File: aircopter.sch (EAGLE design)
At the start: 42 parts, among them IC1 STF202-22T1G, M1 WIRELESS-NRF24L01, U2 GY-521MPU6050, Y1 20 MHz

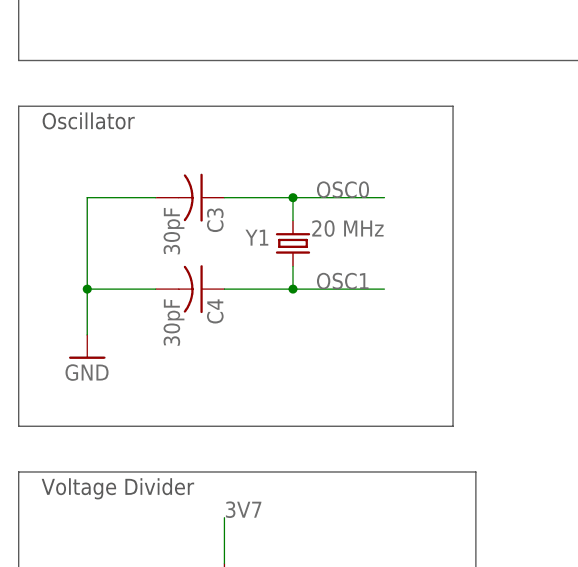
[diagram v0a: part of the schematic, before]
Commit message: changed crystal load capacitance
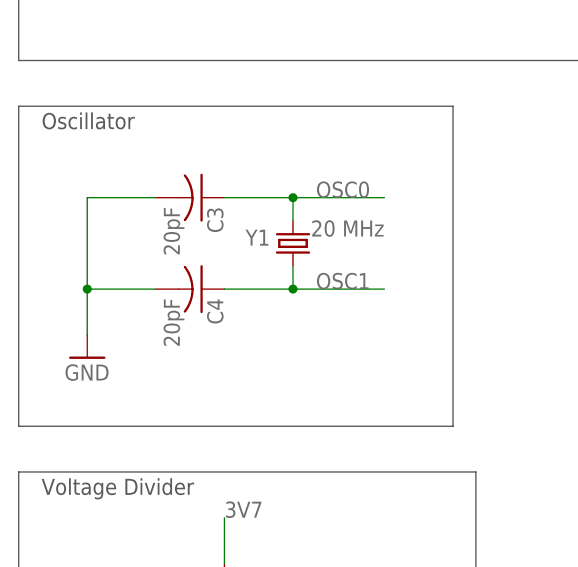
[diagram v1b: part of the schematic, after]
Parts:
- C3, C4: value 30pF -> 20pF
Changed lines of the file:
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@@
 <part name="SUPPLY1" library="Power_Symbols" library_urn="urn:adsk.eagle:library:16502351" deviceset="3V3-CIRCLE" device=""/>
 <part name="SUPPLY2" library="Power_Symbols" library_urn="urn:adsk.eagle:library:16502351" deviceset="3V3-CIRCLE" device=""/>
-<part name="C3" library="rcl" library_urn="urn:adsk.eagle:library:334" deviceset="C-US" device="C0603" package3d_urn="urn:adsk.eagle:package:23616/2" value="30pF"/>
-<part name="C4" library="rcl" library_urn="urn:adsk.eagle:library:334" deviceset="C-US" device="C0603" package3d_urn="urn:adsk.eagle:package:23616/2" value="30pF"/>
+<part name="C3" library="rcl" library_urn="urn:adsk.eagle:library:334" deviceset="C-US" device="C0603" package3d_urn="urn:adsk.eagle:package:23616/2" value="20pF"/>
+<part name="C4" library="rcl" library_urn="urn:adsk.eagle:library:334" deviceset="C-US" device="C0603" package3d_urn="urn:adsk.eagle:package:23616/2" value="20pF"/>
 <part name="GND7" library="IR_Sensor" deviceset="SUPPLY1_GND" device=""/>
 <part name="S1" library="AP_quad" deviceset="SWITCH-MOMENTARY-2" device="SMD"/>

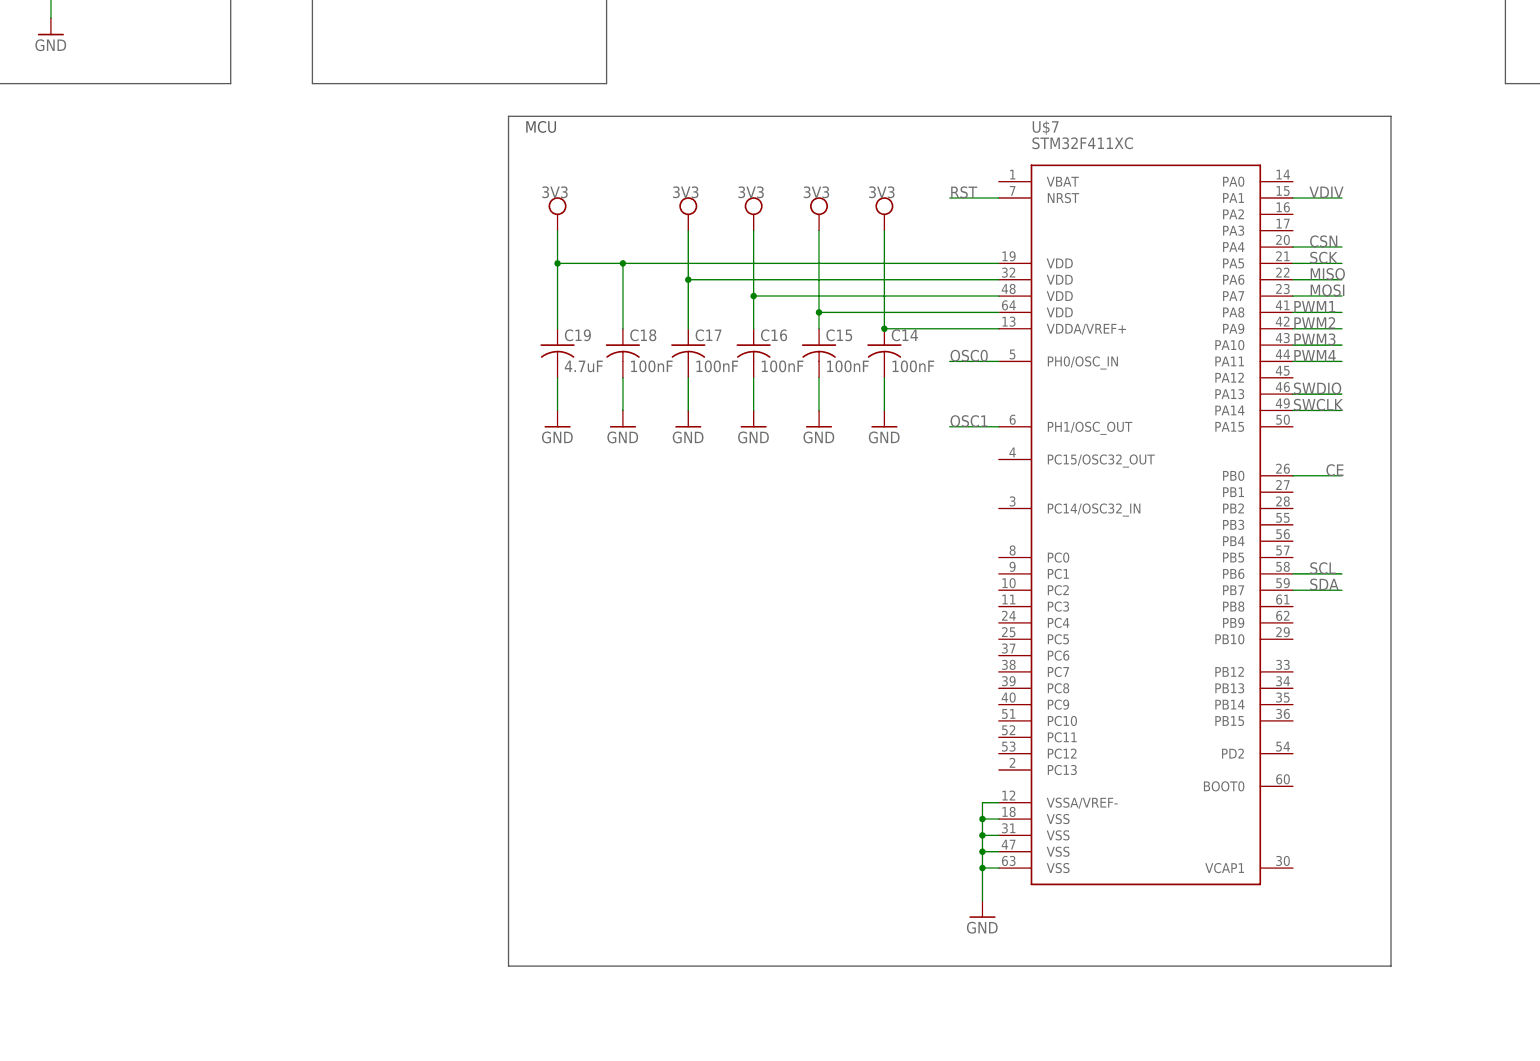
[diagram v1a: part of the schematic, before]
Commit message: minor changes to mcu, added tx/rx headers
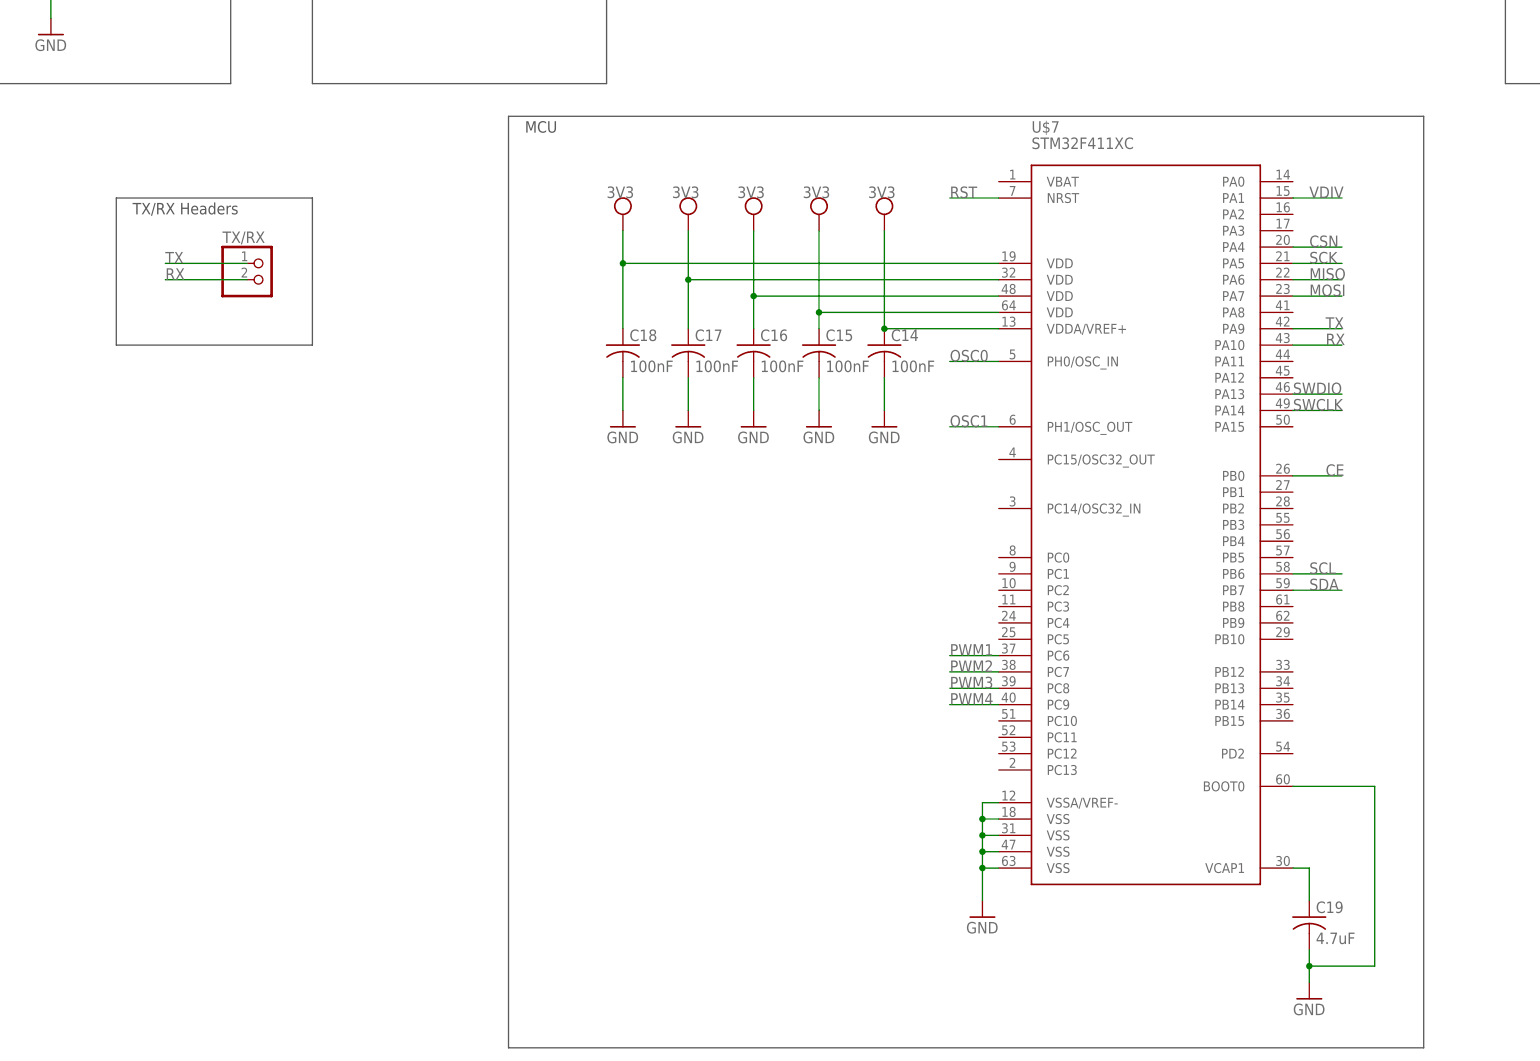
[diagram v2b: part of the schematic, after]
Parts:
- added TX/RX: (no value), pinhead:PINHD-1X2
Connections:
- new net N$7: C19.1, U$7.VCAP1
- new net RX: TX/RX.2, U$7.PA10
- new net TX: TX/RX.1, U$7.PA9
- net 3V3: no longer C19.1
- net GND: now also U$7.BOOT0
- net PWM1: now also U$7.PC6; no longer U$7.PA8
- net PWM2: now also U$7.PC7; no longer U$7.PA9
- net PWM3: now also U$7.PC8; no longer U$7.PA10
- net PWM4: now also U$7.PC9; no longer U$7.PA11
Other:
- note added: "TX/RX Headers"
- moved on the sheet: C19
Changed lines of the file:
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@@
 <part name="SUPPLY11" library="Power_Symbols" library_urn="urn:adsk.eagle:library:16502351" deviceset="3V3-CIRCLE" device=""/>
 <part name="GND22" library="IR_Sensor" deviceset="SUPPLY1_GND" device=""/>
+<part name="TX/RX" library="pinhead" library_urn="urn:adsk.eagle:library:325" deviceset="PINHD-1X2" device="" package3d_urn="urn:adsk.eagle:package:22435/2"/>
 </parts>
 <sheets>
@@
 <wire x1="-109.22" y1="127" x2="-109.22" y2="76.2" width="0.1524" layer="97"/>
 <text x="-106.68" y="124.46" size="1.778" layer="97">Voltage Regulator</text>
-<wire x1="93.98" y1="-83.82" x2="-43.18" y2="-83.82" width="0.1524" layer="97"/>
-<wire x1="-43.18" y1="-83.82" x2="-43.18" y2="-215.9" width="0.1524" layer="97"/>
-<wire x1="-43.18" y1="-215.9" x2="93.98" y2="-215.9" width="0.1524" layer="97"/>
-<wire x1="93.98" y1="-215.9" x2="93.98" y2="-83.82" width="0.1524" layer="97"/>
+<wire x1="99.06" y1="-83.82" x2="-43.18" y2="-83.82" width="0.1524" layer="97"/>
+<wire x1="-43.18" y1="-83.82" x2="-43.18" y2="-228.6" width="0.1524" layer="97"/>
+<wire x1="99.06" y1="-228.6" x2="99.06" y2="-83.82" width="0.1524" layer="97"/>
 <text x="-40.64" y="-86.36" size="1.778" layer="97">MCU</text>
+<wire x1="99.06" y1="-228.6" x2="-43.18" y2="-228.6" width="0.1524" layer="97"/>
+<wire x1="-73.66" y1="-119.38" x2="-104.14" y2="-119.38" width="0.1524" layer="97"/>
+<wire x1="-104.14" y1="-119.38" x2="-104.14" y2="-96.52" width="0.1524" layer="97"/>
+<wire x1="-104.14" y1="-96.52" x2="-73.66" y2="-96.52" width="0.1524" layer="97"/>
+<wire x1="-73.66" y1="-96.52" x2="-73.66" y2="-119.38" width="0.1524" layer="97"/>
+<text x="-101.6" y="-99.06" size="1.778" layer="97">TX/RX Headers</text>
 </plain>
 <instances>
@@
 <attribute name="VALUE" x="-24.384" y="-123.571" size="1.778" layer="96"/>
 </instance>
-<instance part="C19" gate="G$1" x="-35.56" y="-119.38" smashed="yes">
-<attribute name="NAME" x="-34.544" y="-118.745" size="1.778" layer="95"/>
-<attribute name="VALUE" x="-34.544" y="-123.571" size="1.778" layer="96"/>
-</instance>
-<instance part="GND16" gate="1" x="-35.56" y="-132.08" smashed="yes"/>
+<instance part="C19" gate="G$1" x="81.28" y="-208.28" smashed="yes">
+<attribute name="NAME" x="82.296" y="-207.645" size="1.778" layer="95"/>
+<attribute name="VALUE" x="82.296" y="-212.471" size="1.778" layer="96"/>
+</instance>
+<instance part="GND16" gate="1" x="81.28" y="-220.98" smashed="yes"/>
 <instance part="GND17" gate="1" x="-25.4" y="-132.08" smashed="yes"/>
 <instance part="GND18" gate="1" x="-15.24" y="-132.08" smashed="yes"/>
@@
 <instance part="GND20" gate="1" x="5.08" y="-132.08" smashed="yes"/>
 <instance part="GND21" gate="1" x="15.24" y="-132.08" smashed="yes"/>
-<instance part="SUPPLY3" gate="G$1" x="-35.56" y="-99.06" smashed="yes"/>
+<instance part="SUPPLY3" gate="G$1" x="-25.4" y="-99.06" smashed="yes"/>
 <instance part="SUPPLY8" gate="G$1" x="-15.24" y="-99.06" smashed="yes"/>
 <instance part="SUPPLY9" gate="G$1" x="-5.08" y="-99.06" smashed="yes"/>
@@
 <instance part="SUPPLY11" gate="G$1" x="15.24" y="-99.06" smashed="yes"/>
 <instance part="GND22" gate="1" x="30.48" y="-208.28" smashed="yes"/>
+<instance part="TX/RX" gate="G$1" x="-81.28" y="-109.22" smashed="yes">
+<attribute name="NAME" x="-87.63" y="-103.505" size="1.778" layer="95"/>
+<attribute name="VALUE" x="-87.63" y="-114.3" size="1.778" layer="96"/>
+</instance>
 </instances>
 <busses>
@@
 </segment>
 <segment>
-<pinref part="U$7" gate="G$1" pin="PA8"/>
-<wire x1="78.74" y1="-114.3" x2="86.36" y2="-114.3" width="0.1524" layer="91"/>
-<label x="78.74" y="-114.3" size="1.778" layer="95"/>
+<pinref part="U$7" gate="G$1" pin="PC6"/>
+<wire x1="33.02" y1="-167.64" x2="25.4" y2="-167.64" width="0.1524" layer="91"/>
+<label x="25.4" y="-167.64" size="1.778" layer="95"/>
 </segment>
 </net>
@@
 <segment>
 <pinref part="C19" gate="G$1" pin="2"/>
-<wire x1="-35.56" y1="-124.46" x2="-35.56" y2="-129.54" width="0.1524" layer="91"/>
+<wire x1="81.28" y1="-213.36" x2="81.28" y2="-215.9" width="0.1524" layer="91"/>
 <pinref part="GND16" gate="1" pin="GND"/>
-<label x="-38.1" y="-134.62" size="1.778" layer="95"/>
+<label x="78.74" y="-223.52" size="1.778" layer="95"/>
+<pinref part="U$7" gate="G$1" pin="BOOT0"/>
+<wire x1="81.28" y1="-215.9" x2="81.28" y2="-218.44" width="0.1524" layer="91"/>
+<wire x1="78.74" y1="-187.96" x2="91.44" y2="-187.96" width="0.1524" layer="91"/>
+<wire x1="91.44" y1="-187.96" x2="91.44" y2="-215.9" width="0.1524" layer="91"/>
+<wire x1="91.44" y1="-215.9" x2="81.28" y2="-215.9" width="0.1524" layer="91"/>
+<junction x="81.28" y="-215.9"/>
 </segment>
 <segment>
@@
 </segment>
 <segment>
-<pinref part="U$7" gate="G$1" pin="PA9"/>
-<wire x1="78.74" y1="-116.84" x2="86.36" y2="-116.84" width="0.1524" layer="91"/>
-<label x="78.74" y="-116.84" size="1.778" layer="95"/>
+<pinref part="U$7" gate="G$1" pin="PC7"/>
+<wire x1="33.02" y1="-170.18" x2="25.4" y2="-170.18" width="0.1524" layer="91"/>
+<label x="25.4" y="-170.18" size="1.778" layer="95"/>
 </segment>
 </net>
@@
 </segment>
 <segment>
-<pinref part="U$7" gate="G$1" pin="PA10"/>
-<wire x1="78.74" y1="-119.38" x2="86.36" y2="-119.38" width="0.1524" layer="91"/>
-<label x="78.74" y="-119.38" size="1.778" layer="95"/>
+<pinref part="U$7" gate="G$1" pin="PC8"/>
+<wire x1="33.02" y1="-172.72" x2="25.4" y2="-172.72" width="0.1524" layer="91"/>
+<label x="25.4" y="-172.72" size="1.778" layer="95"/>
 </segment>
 </net>
@@
 </segment>
 <segment>
-<pinref part="U$7" gate="G$1" pin="PA11"/>
-<wire x1="78.74" y1="-121.92" x2="86.36" y2="-121.92" width="0.1524" layer="91"/>
-<label x="78.74" y="-121.92" size="1.778" layer="95"/>
+<pinref part="U$7" gate="G$1" pin="PC9"/>
+<wire x1="33.02" y1="-175.26" x2="25.4" y2="-175.26" width="0.1524" layer="91"/>
+<label x="25.4" y="-175.26" size="1.778" layer="95"/>
 </segment>
 </net>
@@
 </segment>
 <segment>
-<pinref part="U$7" gate="G$1" pin="VDD@1"/>
-<wire x1="33.02" y1="-106.68" x2="-25.4" y2="-106.68" width="0.1524" layer="91"/>
-<pinref part="C18" gate="G$1" pin="1"/>
-<wire x1="-25.4" y1="-106.68" x2="-35.56" y2="-106.68" width="0.1524" layer="91"/>
-<wire x1="-25.4" y1="-106.68" x2="-25.4" y2="-116.84" width="0.1524" layer="91"/>
-<junction x="-25.4" y="-106.68"/>
-<pinref part="C19" gate="G$1" pin="1"/>
-<wire x1="-35.56" y1="-106.68" x2="-35.56" y2="-116.84" width="0.1524" layer="91"/>
-<wire x1="-35.56" y1="-106.68" x2="-35.56" y2="-101.6" width="0.1524" layer="91"/>
-<junction x="-35.56" y="-106.68"/>
-<pinref part="SUPPLY3" gate="G$1" pin="+V"/>
-<label x="-38.1" y="-96.52" size="1.778" layer="95"/>
-</segment>
-<segment>
 <pinref part="U$7" gate="G$1" pin="VDD@2"/>
 <wire x1="33.02" y1="-109.22" x2="-15.24" y2="-109.22" width="0.1524" layer="91"/>
@@
 <pinref part="SUPPLY11" gate="G$1" pin="+V"/>
 <label x="12.7" y="-96.52" size="1.778" layer="95"/>
+</segment>
+<segment>
+<pinref part="U$7" gate="G$1" pin="VDD@1"/>
+<wire x1="33.02" y1="-106.68" x2="-25.4" y2="-106.68" width="0.1524" layer="91"/>
+<pinref part="C18" gate="G$1" pin="1"/>
+<wire x1="-25.4" y1="-106.68" x2="-25.4" y2="-116.84" width="0.1524" layer="91"/>
+<wire x1="-25.4" y1="-106.68" x2="-25.4" y2="-101.6" width="0.1524" layer="91"/>
+<junction x="-25.4" y="-106.68"/>
+<pinref part="SUPPLY3" gate="G$1" pin="+V"/>
+<label x="-27.94" y="-96.52" size="1.778" layer="95"/>
 </segment>
 </net>
@@
 </segment>
 </net>
+<net name="N$7" class="0">
+<segment>
+<pinref part="U$7" gate="G$1" pin="VCAP1"/>
+<pinref part="C19" gate="G$1" pin="1"/>
+<wire x1="78.74" y1="-200.66" x2="81.28" y2="-200.66" width="0.1524" layer="91"/>
+<wire x1="81.28" y1="-200.66" x2="81.28" y2="-205.74" width="0.1524" layer="91"/>
+</segment>
+</net>
+<net name="TX" class="0">
+<segment>
+<pinref part="U$7" gate="G$1" pin="PA9"/>
+<wire x1="78.74" y1="-116.84" x2="86.36" y2="-116.84" width="0.1524" layer="91"/>
+<label x="83.82" y="-116.84" size="1.778" layer="95"/>
+</segment>
+<segment>
+<pinref part="TX/RX" gate="G$1" pin="1"/>
+<wire x1="-83.82" y1="-106.68" x2="-96.52" y2="-106.68" width="0.1524" layer="91"/>
+<label x="-96.52" y="-106.68" size="1.778" layer="95"/>
+</segment>
+</net>
+<net name="RX" class="0">
+<segment>
+<pinref part="U$7" gate="G$1" pin="PA10"/>
+<wire x1="78.74" y1="-119.38" x2="86.36" y2="-119.38" width="0.1524" layer="91"/>
+<label x="83.82" y="-119.38" size="1.778" layer="95"/>
+</segment>
+<segment>
+<pinref part="TX/RX" gate="G$1" pin="2"/>
+<wire x1="-83.82" y1="-109.22" x2="-96.52" y2="-109.22" width="0.1524" layer="91"/>
+<label x="-96.52" y="-109.22" size="1.778" layer="95"/>
+</segment>
+</net>
